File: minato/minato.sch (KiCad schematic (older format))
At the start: 421 parts

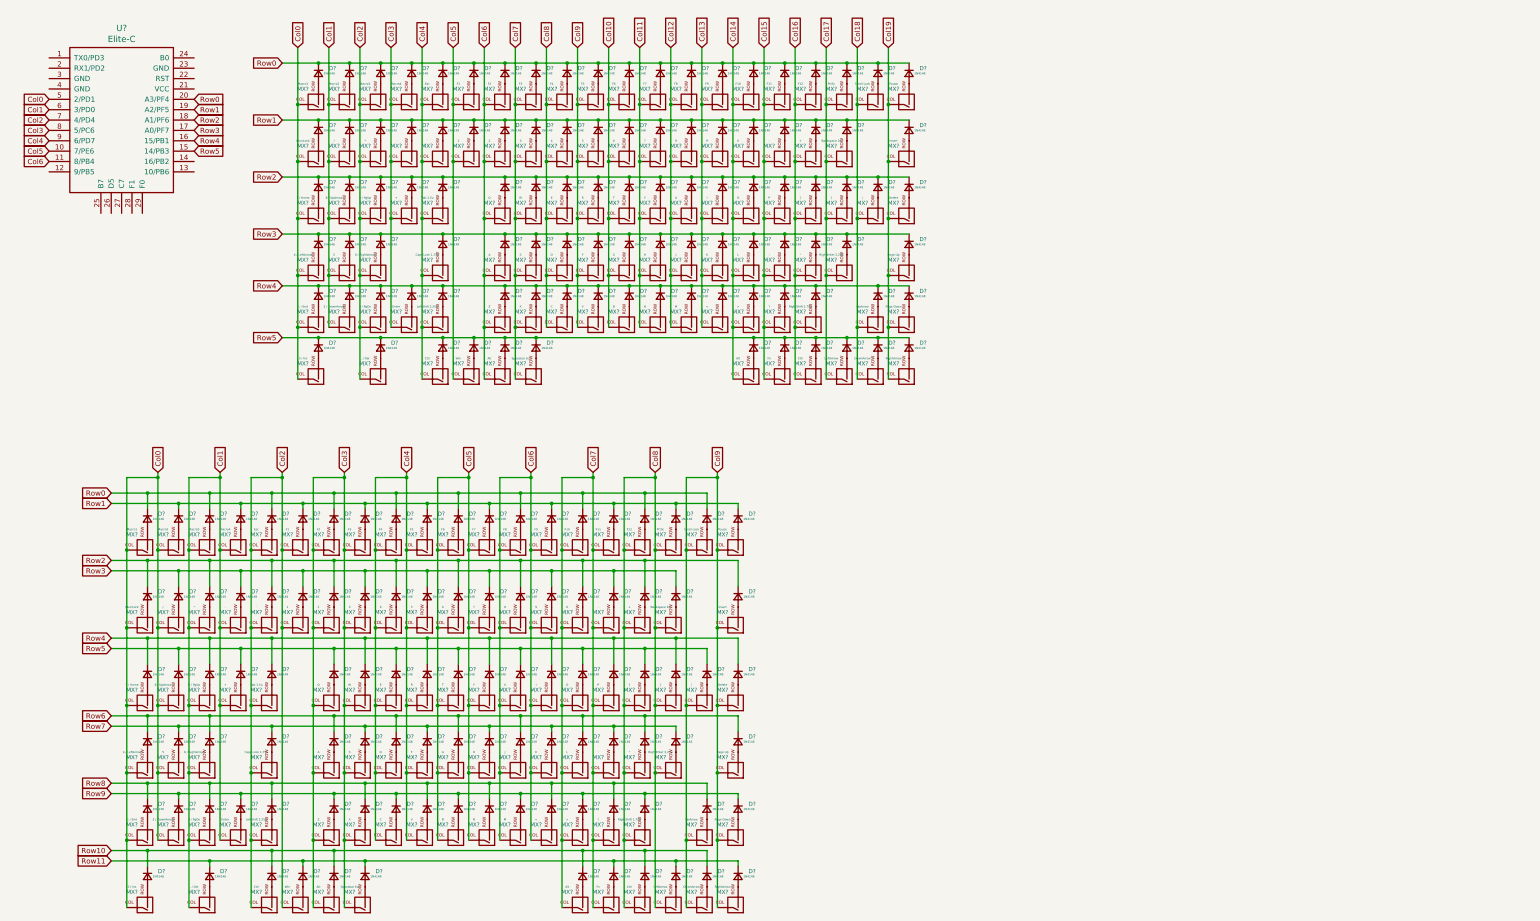
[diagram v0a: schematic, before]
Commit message: :sparkles: Add global labels
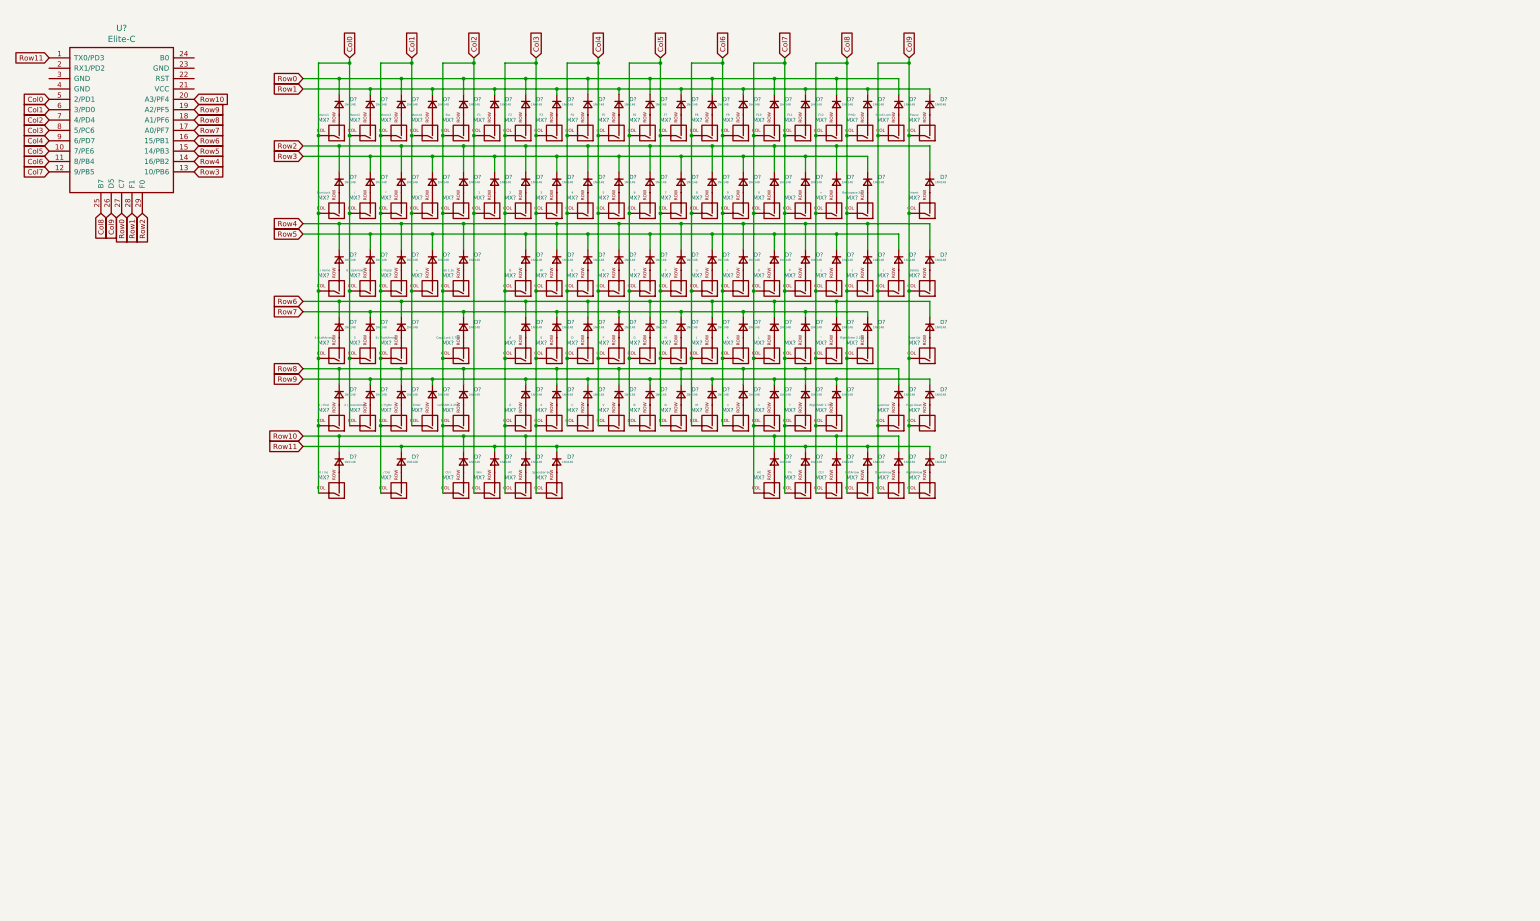
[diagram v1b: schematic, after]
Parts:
- removed D? (x105): 1N4148, symbol Device:D_Small
- removed MX?: Macro1, symbol MX_Alps_Hybrid:MX-NoLED
- removed MX?: Macro2, symbol MX_Alps_Hybrid:MX-NoLED
- removed MX?: Macro3, symbol MX_Alps_Hybrid:MX-NoLED
- removed MX?: Macro4, symbol MX_Alps_Hybrid:MX-NoLED
- removed MX?: NumLock, symbol MX_Alps_Hybrid:MX-NoLED
- removed MX?: /, symbol MX_Alps_Hybrid:MX-NoLED
- removed MX?: *, symbol MX_Alps_Hybrid:MX-NoLED
- removed MX? (x2): -, symbol MX_Alps_Hybrid:MX-NoLED
- removed MX?: 7 / Home, symbol MX_Alps_Hybrid:MX-NoLED
- removed MX?: 8 / UpArrow, symbol MX_Alps_Hybrid:MX-NoLED
- removed MX?: 9 / PgUp, symbol MX_Alps_Hybrid:MX-NoLED
- removed MX?: 4 / LeftArrow, symbol MX_Alps_Hybrid:MX-NoLED
- removed MX? (x2): 5, symbol MX_Alps_Hybrid:MX-NoLED
- removed MX?: 6 / RightArrow, symbol MX_Alps_Hybrid:MX-NoLED
- removed MX? (x2): +, symbol MX_Alps_Hybrid:MX-NoLED
- removed MX?: 1 / End, symbol MX_Alps_Hybrid:MX-NoLED
- removed MX?: 2 / DownArrow, symbol MX_Alps_Hybrid:MX-NoLED
- removed MX?: 3 / PgDn, symbol MX_Alps_Hybrid:MX-NoLED
- removed MX?: Enter, symbol MX_Alps_Hybrid:MX-NoLED
- removed MX?: 0 / Ins, symbol MX_Alps_Hybrid:MX-NoLED
- removed MX?: . / Del, symbol MX_Alps_Hybrid:MX-NoLED
- removed MX?: Esc, symbol MX_Alps_Hybrid:MX-NoLED
- removed MX?: `, symbol MX_Alps_Hybrid:MX-NoLED
- removed MX?: Tab 1.5u, symbol MX_Alps_Hybrid:MX-NoLED
- removed MX?: Caps Lock 1.75u, symbol MX_Alps_Hybrid:MX-NoLED
- removed MX?: LeftShift 2.25u, symbol MX_Alps_Hybrid:MX-NoLED
- removed MX? (x2): Ctrl, symbol MX_Alps_Hybrid:MX-NoLED
- removed MX?: F1, symbol MX_Alps_Hybrid:MX-NoLED
- removed MX?: 1, symbol MX_Alps_Hybrid:MX-NoLED
- removed MX?: Win, symbol MX_Alps_Hybrid:MX-NoLED
- removed MX?: F2, symbol MX_Alps_Hybrid:MX-NoLED
- removed MX?: 2, symbol MX_Alps_Hybrid:MX-NoLED
- removed MX?: Q, symbol MX_Alps_Hybrid:MX-NoLED
- removed MX?: A, symbol MX_Alps_Hybrid:MX-NoLED
- removed MX?: Z, symbol MX_Alps_Hybrid:MX-NoLED
- removed MX? (x2): Alt, symbol MX_Alps_Hybrid:MX-NoLED
- removed MX?: F3, symbol MX_Alps_Hybrid:MX-NoLED
- removed MX?: 3, symbol MX_Alps_Hybrid:MX-NoLED
- removed MX?: W, symbol MX_Alps_Hybrid:MX-NoLED
- removed MX?: S, symbol MX_Alps_Hybrid:MX-NoLED
- removed MX?: X, symbol MX_Alps_Hybrid:MX-NoLED
- removed MX?: Spacebar 6u, symbol MX_Alps_Hybrid:MX-NoLED
- removed MX?: F4, symbol MX_Alps_Hybrid:MX-NoLED
- removed MX?: 4, symbol MX_Alps_Hybrid:MX-NoLED
- removed MX?: E, symbol MX_Alps_Hybrid:MX-NoLED
- removed MX?: D, symbol MX_Alps_Hybrid:MX-NoLED
- removed MX?: C, symbol MX_Alps_Hybrid:MX-NoLED
- removed MX?: F5, symbol MX_Alps_Hybrid:MX-NoLED
- removed MX?: R, symbol MX_Alps_Hybrid:MX-NoLED
- removed MX?: F, symbol MX_Alps_Hybrid:MX-NoLED
- removed MX?: V, symbol MX_Alps_Hybrid:MX-NoLED
- removed MX?: F6, symbol MX_Alps_Hybrid:MX-NoLED
- removed MX?: 6, symbol MX_Alps_Hybrid:MX-NoLED
- removed MX?: T, symbol MX_Alps_Hybrid:MX-NoLED
- removed MX?: G, symbol MX_Alps_Hybrid:MX-NoLED
- removed MX?: B, symbol MX_Alps_Hybrid:MX-NoLED
- removed MX?: F7, symbol MX_Alps_Hybrid:MX-NoLED
- removed MX?: 7, symbol MX_Alps_Hybrid:MX-NoLED
- removed MX?: Y, symbol MX_Alps_Hybrid:MX-NoLED
- removed MX?: H, symbol MX_Alps_Hybrid:MX-NoLED
- removed MX?: N, symbol MX_Alps_Hybrid:MX-NoLED
- removed MX?: F8, symbol MX_Alps_Hybrid:MX-NoLED
- removed MX?: 8, symbol MX_Alps_Hybrid:MX-NoLED
- removed MX?: U, symbol MX_Alps_Hybrid:MX-NoLED
- removed MX?: J, symbol MX_Alps_Hybrid:MX-NoLED
- removed MX?: M, symbol MX_Alps_Hybrid:MX-NoLED
- removed MX?: F9, symbol MX_Alps_Hybrid:MX-NoLED
- removed MX?: 9, symbol MX_Alps_Hybrid:MX-NoLED
- removed MX?: I, symbol MX_Alps_Hybrid:MX-NoLED
- removed MX?: K, symbol MX_Alps_Hybrid:MX-NoLED
- removed MX?: <, symbol MX_Alps_Hybrid:MX-NoLED
- removed MX?: F10, symbol MX_Alps_Hybrid:MX-NoLED
- removed MX?: 0, symbol MX_Alps_Hybrid:MX-NoLED
- removed MX?: O, symbol MX_Alps_Hybrid:MX-NoLED
- removed MX?: L, symbol MX_Alps_Hybrid:MX-NoLED
- removed MX?: >, symbol MX_Alps_Hybrid:MX-NoLED
- removed MX?: F11, symbol MX_Alps_Hybrid:MX-NoLED
- removed MX?: P, symbol MX_Alps_Hybrid:MX-NoLED
- removed MX?: :, symbol MX_Alps_Hybrid:MX-NoLED
- removed MX?: ?, symbol MX_Alps_Hybrid:MX-NoLED
- removed MX?: Fn, symbol MX_Alps_Hybrid:MX-NoLED
- removed MX?: F12, symbol MX_Alps_Hybrid:MX-NoLED
- removed MX?: {, symbol MX_Alps_Hybrid:MX-NoLED
- removed MX?: \", symbol MX_Alps_Hybrid:MX-NoLED
- removed MX?: RightShift 1.75u, symbol MX_Alps_Hybrid:MX-NoLED
- removed MX?: PrtSc, symbol MX_Alps_Hybrid:MX-NoLED
- removed MX?: Backspace 2u, symbol MX_Alps_Hybrid:MX-NoLED
- removed MX?: }, symbol MX_Alps_Hybrid:MX-NoLED
- removed MX?: RightEnter 2.25u, symbol MX_Alps_Hybrid:MX-NoLED
- removed MX?: LeftArrow, symbol MX_Alps_Hybrid:MX-NoLED
- removed MX?: Scroll Lock, symbol MX_Alps_Hybrid:MX-NoLED
- removed MX?: |, symbol MX_Alps_Hybrid:MX-NoLED
- removed MX?: UpArrow, symbol MX_Alps_Hybrid:MX-NoLED
- removed MX?: DownArrow, symbol MX_Alps_Hybrid:MX-NoLED
- removed MX?: Pause, symbol MX_Alps_Hybrid:MX-NoLED
- removed MX?: Insert, symbol MX_Alps_Hybrid:MX-NoLED
- removed MX?: Delete, symbol MX_Alps_Hybrid:MX-NoLED
- removed MX?: Page Up, symbol MX_Alps_Hybrid:MX-NoLED
- removed MX?: Page Down, symbol MX_Alps_Hybrid:MX-NoLED
- removed MX?: RightArrow, symbol MX_Alps_Hybrid:MX-NoLED
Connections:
- net Col7: now also U?.12 (9/PB5)
- net Col8: now also U?.25 (B7)
- net Col9: now also U?.26 (D5)
- net Row0: now also U?.27 (C7); no longer U?.20 (A3/PF4)
- net Row1: now also U?.28 (F1); no longer U?.19 (A2/PF5)
- net Row10: now also U?.20 (A3/PF4)
- net Row11: now also U?.1 (TX0/PD3)
- net Row2: now also U?.29 (F0); no longer U?.18 (A1/PF6)
- net Row3: now also U?.13 (10/PB6); no longer U?.17 (A0/PF7)
- net Row4: now also U?.14 (16/PB2); no longer U?.16 (15/PB1)
- net Row6: now also U?.16 (15/PB1)
- net Row7: now also U?.17 (A0/PF7)
- net Row8: now also U?.18 (A1/PF6)
- net Row9: now also U?.19 (A2/PF5)
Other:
- moved on the sheet: D?, MX?

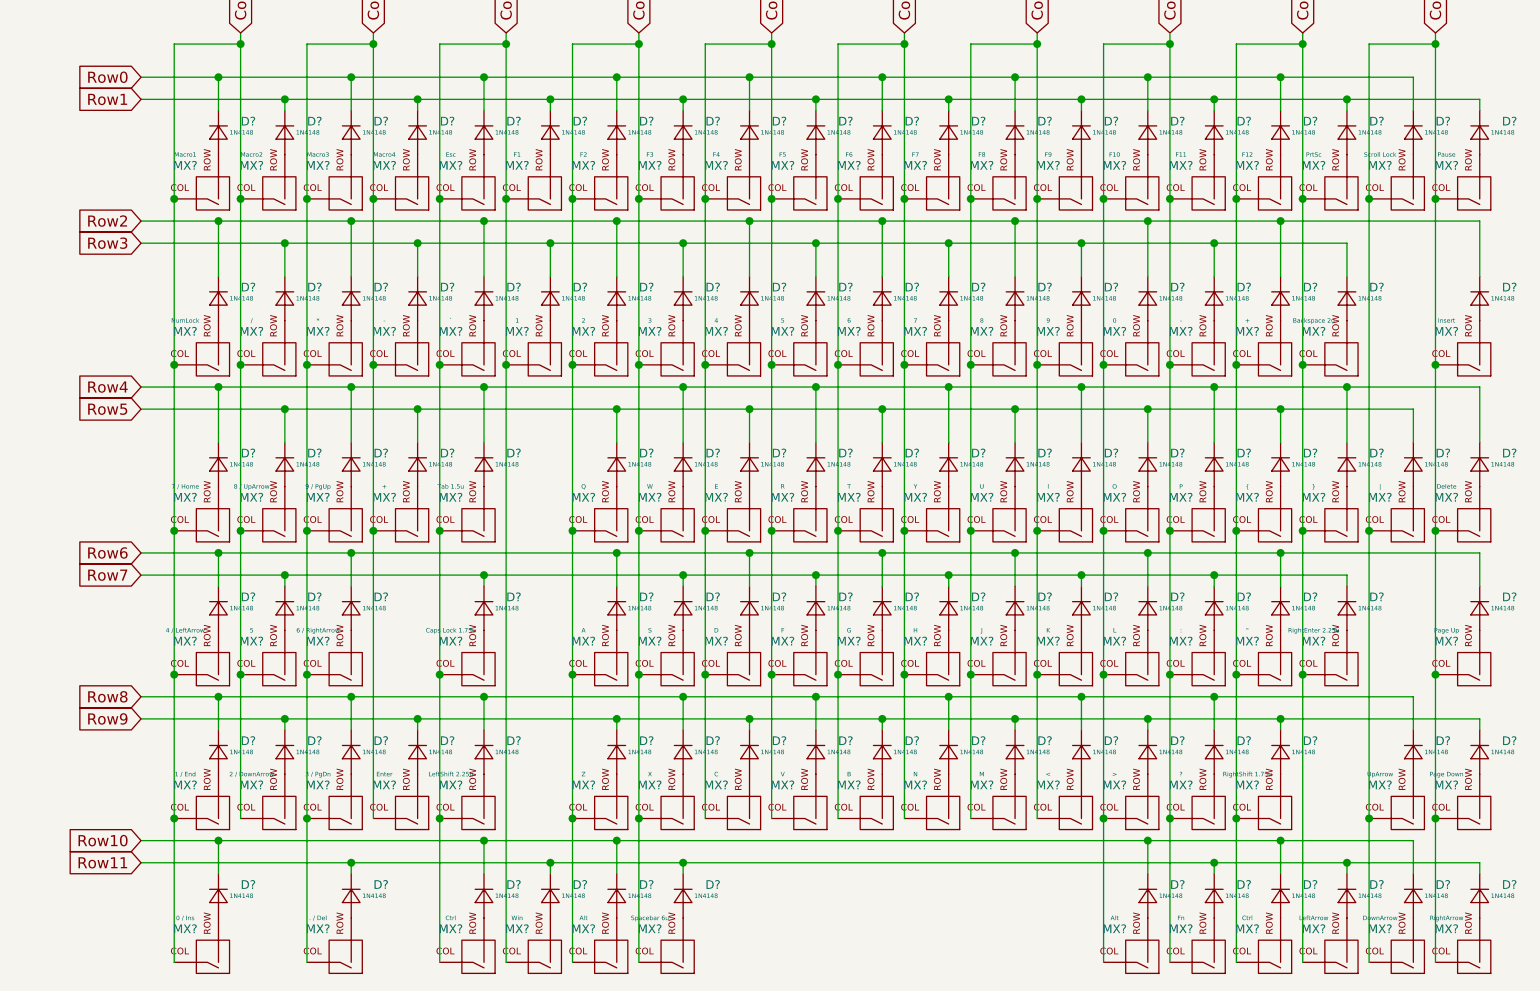
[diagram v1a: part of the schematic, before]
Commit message: :sparkles: Name reference switches
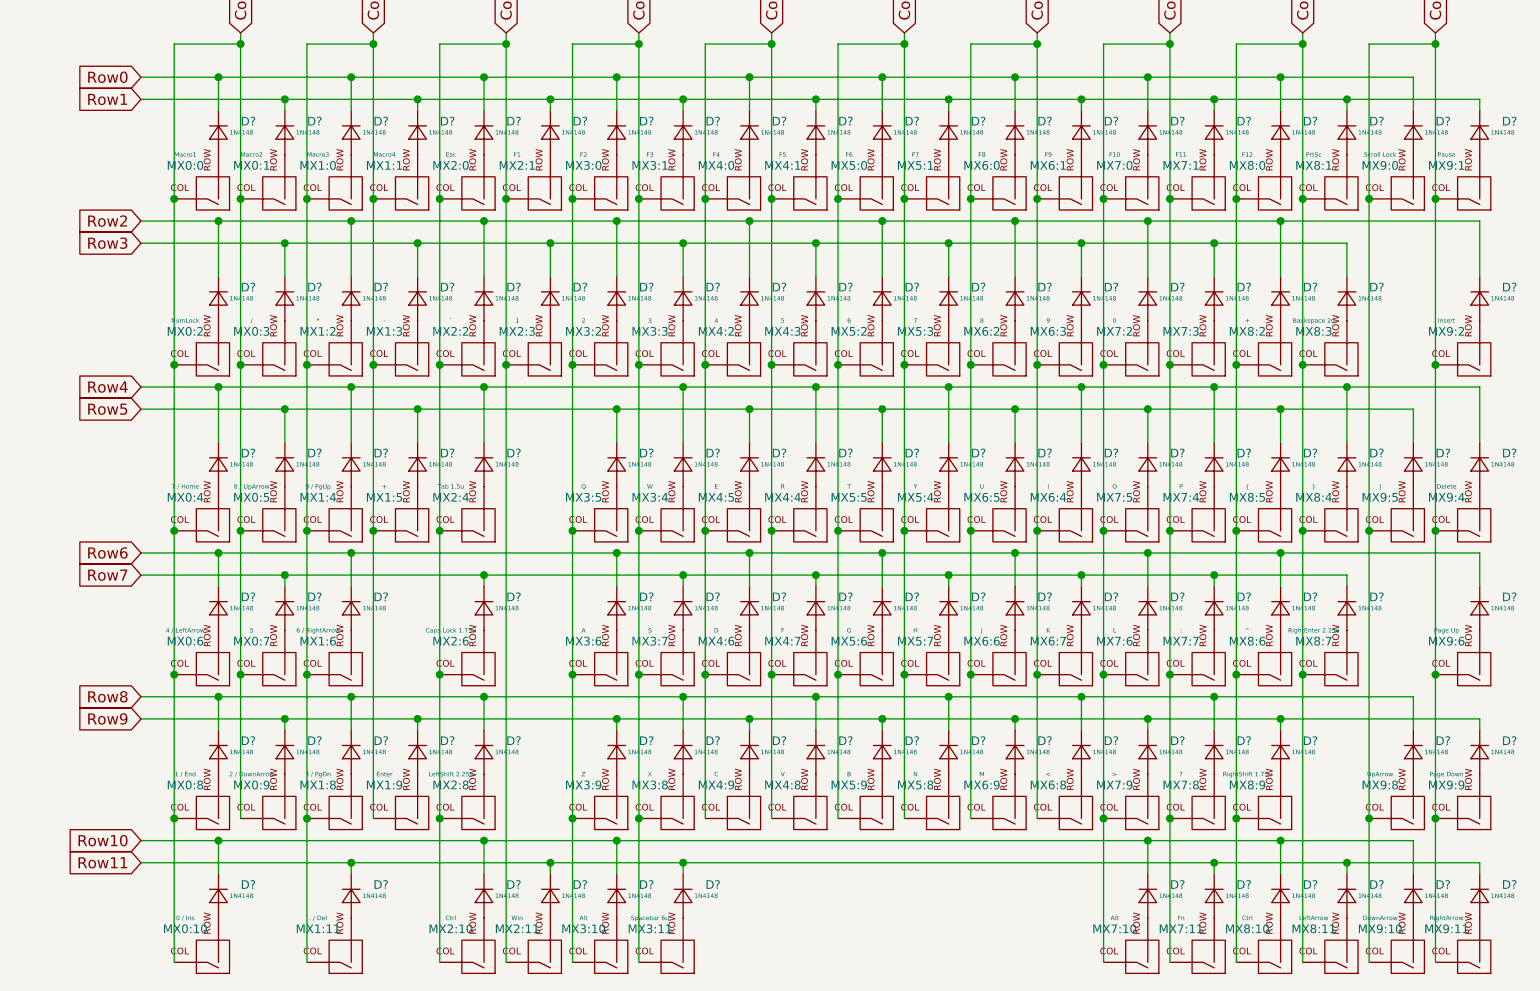
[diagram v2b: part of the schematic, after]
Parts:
- gave numbers to parts that had none: 105

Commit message: :sparkles: Map schematics to footprints
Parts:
- D1, D10, D100, D101, D102, D103, D104, D105, D11, D12, D13, D14, D15, D16, D17, D18, D19, D2, D20, D21, D22, D23, D24, D25, D26, D27, D28, D29, D3, D30, D31, D32, D33, D34, D35, D36, D37, D38, D39, D4, D40, D41, D42, D43, D44, D45, D46, D47, D48, D49, D5, D50, D51, D52, D53, D54, D55, D56, D57, D58, D59, D6, D60, D61, D62, D63, D64, D65, D66, D67, D68, D69, D7, D70, D71, D72, D73, D74, D75, D76, D77, D78, D79, D8, D80, D81, D82, D83, D84, D85, D86, D87, D88, D89, D9, D90, D91, D92, D93, D94, D95, D96, D97, D98, D99: renamed from D?; footprint (none) -> Diode_SMD:D_SOD-123
- MX0:0, MX0:1, MX0:10, MX0:2, MX0:3, MX0:4, MX0:5, MX0:6, MX0:7, MX0:8, MX0:9, MX1:0, MX1:1, MX1:11, MX1:2, MX1:3, MX1:4, MX1:5, MX1:6, MX1:8, MX1:9, MX2:0, MX2:1, MX2:10, MX2:11, MX2:2, MX2:3, MX2:4, MX2:6, MX2:8, MX3:0, MX3:1, MX3:10, MX3:11, MX3:2, MX3:3, MX3:4, MX3:5, MX3:6, MX3:7, MX3:8, MX3:9, MX4:0, MX4:1, MX4:2, MX4:3, MX4:4, MX4:5, MX4:6, MX4:7, MX4:8, MX4:9, MX5:0, MX5:1, MX5:2, MX5:3, MX5:4, MX5:5, MX5:6, MX5:7, MX5:8, MX5:9, MX6:0, MX6:1, MX6:2, MX6:3, MX6:4, MX6:5, MX6:6, MX6:7, MX6:8, MX6:9, MX7:0, MX7:1, MX7:10, MX7:11, MX7:2, MX7:3, MX7:4, MX7:5, MX7:6, MX7:7, MX7:8, MX7:9, MX8:0, MX8:1, MX8:10, MX8:11, MX8:2, MX8:3, MX8:4, MX8:5, MX8:6, MX8:7, MX8:9, MX9:0, MX9:1, MX9:10, MX9:11, MX9:2, MX9:4, MX9:5, MX9:6, MX9:8, MX9:9: footprint (none) -> keyswitches.pretty:Kailh_socket_MX
- U1: renamed from U?; footprint (none) -> Keebio-Parts.pretty:Elite-C
